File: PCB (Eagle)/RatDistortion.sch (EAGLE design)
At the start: 44 parts, among them IC1 LM308D

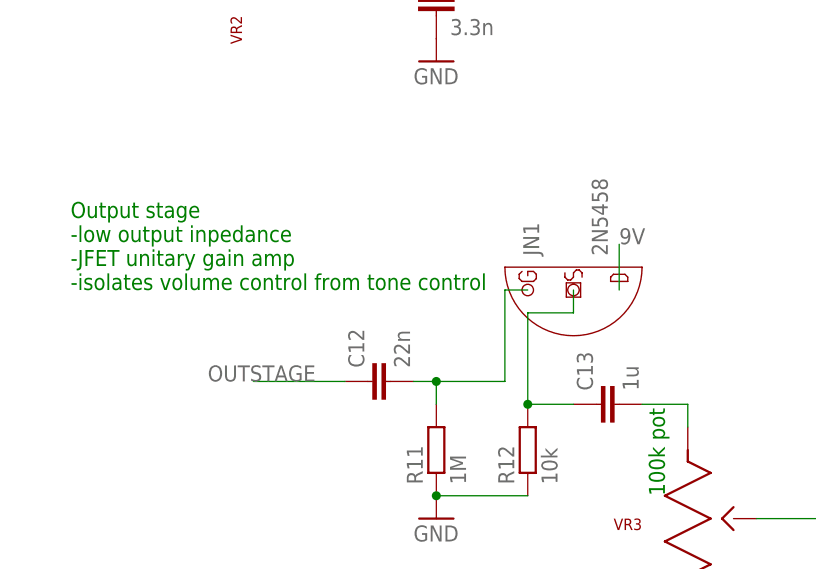
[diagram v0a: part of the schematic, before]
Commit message: Updated Eagle files
JFET 2N5458 (Q1 (was JN1)) in schematic is now correct icon (used default J201 device (same package and pinout)
Updated PCB to Q1 and made values more readable for documentation (Value will probably not be printed on Silk layer)
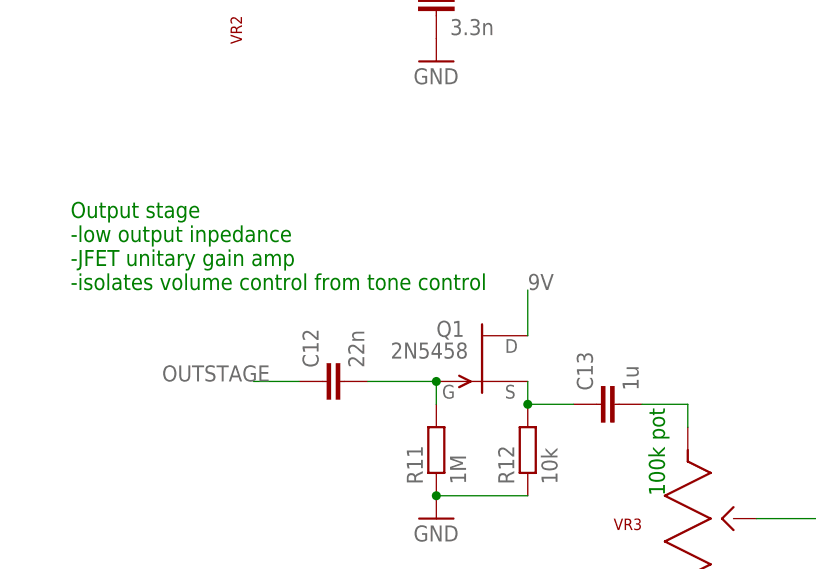
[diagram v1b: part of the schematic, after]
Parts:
- removed JN1: 2N5458, 2N5458:2N5458
- added Q1: 2N5458, transistor-fet:J201
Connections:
- removed net N$17: C13.1, JN1.S, R12.2
- new net N$11: C13.1, Q1.S, R12.2
- net 9V: now also Q1.D; no longer JN1.D
- net N$8: now also Q1.G; no longer JN1.G
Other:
- moved on the sheet: C12
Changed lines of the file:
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@@
 <part name="VR2" library="PTV09A-4225F-B104" deviceset="PTV09A-4225F-B104" device=""/>
 <part name="VR3" library="PTV09A-4225F-B104" deviceset="PTV09A-4225F-B104" device=""/>
-<part name="JN1" library="2N5458" deviceset="2N5458" device=""/>
 <part name="F1" library="adafruit" library_urn="urn:adsk.eagle:library:420" deviceset="PTCFUSE" device="-1812" package3d_urn="urn:adsk.eagle:package:6240348/1" value="100mA"/>
+<part name="Q1" library="transistor-fet" library_urn="urn:adsk.eagle:library:396" deviceset="?20*" device="J" package3d_urn="urn:adsk.eagle:package:28523/2" technology="1" value="2N5458"/>
 </parts>
 <sheets>
@@
 <attribute name="VALUE" x="17.78" y="-30.48" size="1.778" layer="96"/>
 </instance>
-<instance part="C12" gate="G$1" x="12.7" y="-63.5" smashed="yes" rot="R90">
-<attribute name="NAME" x="12.319" y="-61.976" size="1.778" layer="95" rot="R90"/>
-<attribute name="VALUE" x="17.399" y="-61.976" size="1.778" layer="96" rot="R90"/>
+<instance part="C12" gate="G$1" x="7.62" y="-63.5" smashed="yes" rot="R90">
+<attribute name="NAME" x="7.239" y="-61.976" size="1.778" layer="95" rot="R90"/>
+<attribute name="VALUE" x="12.319" y="-61.976" size="1.778" layer="96" rot="R90"/>
 </instance>
 <instance part="R11" gate="G$1" x="20.32" y="-71.12" smashed="yes" rot="R90">
@@
 <attribute name="NAME" x="43.18" y="-78.74" size="1.27" layer="94" rot="R180"/>
 </instance>
-<instance part="JN1" gate="G$1" x="35.56" y="-53.34" smashed="yes" rot="R90">
-<attribute name="NAME" x="31.749859375" y="-49.529859375" size="1.77806875" layer="95" rot="R90"/>
-<attribute name="VALUE" x="39.373059375" y="-49.526940625" size="1.77943125" layer="96" rot="R90"/>
-</instance>
 <instance part="F1" gate="G$1" x="2.54" y="15.24" smashed="yes">
 <attribute name="VALUE" x="-1.27" y="13.97" size="1.778" layer="96"/>
 <attribute name="NAME" x="-1.27" y="20.32" size="1.778" layer="95"/>
+</instance>
+<instance part="Q1" gate="G$1" x="25.4" y="-60.96" smashed="yes">
+<attribute name="NAME" x="20.32" y="-58.547" size="1.778" layer="95"/>
+<attribute name="VALUE" x="15.24" y="-60.96" size="1.778" layer="96"/>
 </instance>
 </instances>
@@
 </segment>
 <segment>
-<label x="40.64" y="-48.26" size="1.778" layer="95"/>
-<pinref part="JN1" gate="G$1" pin="D"/>
-<wire x1="40.64" y1="-48.26" x2="40.64" y2="-53.34" width="0.1524" layer="91"/>
+<label x="30.48" y="-53.34" size="1.778" layer="95"/>
+<wire x1="30.48" y1="-53.34" x2="30.48" y2="-58.42" width="0.1524" layer="91"/>
+<pinref part="Q1" gate="G$1" pin="D"/>
 </segment>
 <segment>
@@
 <segment>
 <pinref part="C12" gate="G$1" pin="1"/>
-<wire x1="10.16" y1="-63.5" x2="0" y2="-63.5" width="0.1524" layer="91"/>
-<label x="-5.08" y="-63.5" size="1.778" layer="95"/>
+<wire x1="5.08" y1="-63.5" x2="0" y2="-63.5" width="0.1524" layer="91"/>
+<label x="-10.16" y="-63.5" size="1.778" layer="95"/>
 </segment>
 </net>
@@
 <pinref part="C12" gate="G$1" pin="2"/>
 <pinref part="R11" gate="G$1" pin="2"/>
-<wire x1="17.78" y1="-63.5" x2="20.32" y2="-63.5" width="0.1524" layer="91"/>
+<wire x1="12.7" y1="-63.5" x2="20.32" y2="-63.5" width="0.1524" layer="91"/>
 <wire x1="20.32" y1="-63.5" x2="20.32" y2="-66.04" width="0.1524" layer="91"/>
-<wire x1="20.32" y1="-63.5" x2="27.94" y2="-63.5" width="0.1524" layer="91"/>
+<pinref part="Q1" gate="G$1" pin="G"/>
 <junction x="20.32" y="-63.5"/>
-<wire x1="27.94" y1="-63.5" x2="27.94" y2="-53.34" width="0.1524" layer="91"/>
-<pinref part="JN1" gate="G$1" pin="G"/>
-<wire x1="27.94" y1="-53.34" x2="30.48" y2="-53.34" width="0.1524" layer="91"/>
-</segment>
-</net>
-<net name="N$17" class="0">
-<segment>
-<pinref part="C13" gate="G$1" pin="1"/>
-<pinref part="R12" gate="G$1" pin="2"/>
-<wire x1="35.56" y1="-66.04" x2="30.48" y2="-66.04" width="0.1524" layer="91"/>
-<junction x="30.48" y="-66.04"/>
-<wire x1="30.48" y1="-66.04" x2="30.48" y2="-55.88" width="0.1524" layer="91"/>
-<wire x1="30.48" y1="-55.88" x2="35.56" y2="-55.88" width="0.1524" layer="91"/>
-<pinref part="JN1" gate="G$1" pin="S"/>
-<wire x1="35.56" y1="-55.88" x2="35.56" y2="-53.34" width="0.1524" layer="91"/>
 </segment>
 </net>
@@
 </segment>
 </net>
+<net name="N$11" class="0">
+<segment>
+<pinref part="R12" gate="G$1" pin="2"/>
+<pinref part="C13" gate="G$1" pin="1"/>
+<wire x1="35.56" y1="-66.04" x2="30.48" y2="-66.04" width="0.1524" layer="91"/>
+<junction x="30.48" y="-66.04"/>
+<wire x1="30.48" y1="-66.04" x2="30.48" y2="-63.5" width="0.1524" layer="91"/>
+<pinref part="Q1" gate="G$1" pin="S"/>
+</segment>
+</net>

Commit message: Moved Q1 to own lib Eagle files
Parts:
- Q1: device transistor-fet:J201 -> 2N5458_2:2N5458TO92
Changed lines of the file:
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@@
 <part name="VR3" library="PTV09A-4225F-B104" deviceset="PTV09A-4225F-B104" device=""/>
 <part name="F1" library="adafruit" library_urn="urn:adsk.eagle:library:420" deviceset="PTCFUSE" device="-1812" package3d_urn="urn:adsk.eagle:package:6240348/1" value="100mA"/>
-<part name="Q1" library="transistor-fet" library_urn="urn:adsk.eagle:library:396" deviceset="?20*" device="J" package3d_urn="urn:adsk.eagle:package:28523/2" technology="1" value="2N5458"/>
+<part name="Q1" library="2N5458_2" deviceset="2N5458" device="TO92" package3d_urn="urn:adsk.eagle:package:28523/2" value="2N5458"/>
 </parts>
 <sheets>
